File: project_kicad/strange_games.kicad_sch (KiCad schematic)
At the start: 131 parts, among them J1 Display, M1 Motor_DC, Q1 Si2302A, Q2 Q_Photo, Q3 Si2302A, Q4 Q_Photo, SW1 SW_Push, SW10 SW_Push, SW11 SW_Push, SW2 SW_Push, SW3 SW_Push, SW4 SW_Push, SW5 SW_Push, SW6 SW_Push, SW7 SW_Push, SW8 SW_Push, SW9 SW_Push, U1 charge controller, U2 boost converter, U3 LDL1117S33R, U4 ESP32-DEVKIT-V1, U5 TMP112xxDRL, U6 vibrating_sensor, U7 LSM6DS3, U8 MQ-135 gas sensor

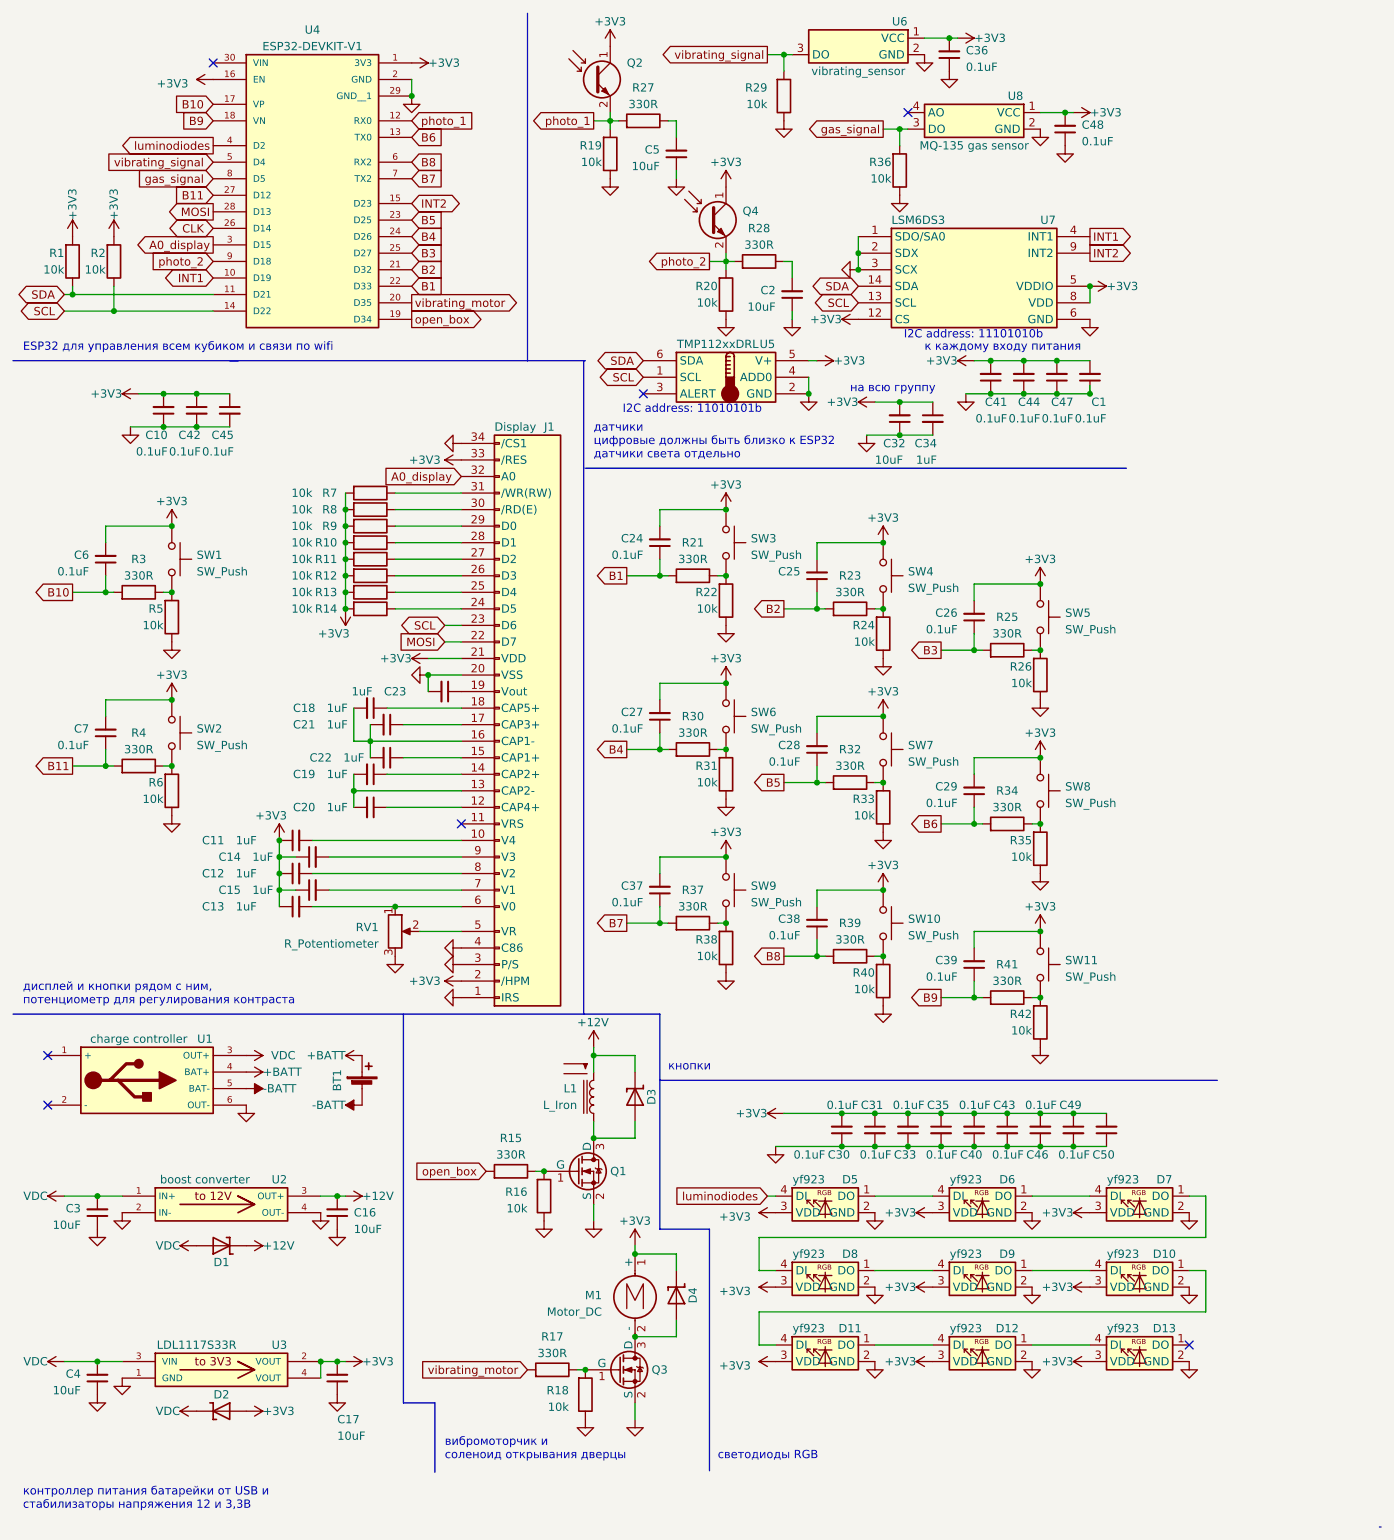
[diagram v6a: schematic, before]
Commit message: pcb changes
deleted resistor from unused pins because they take so much place
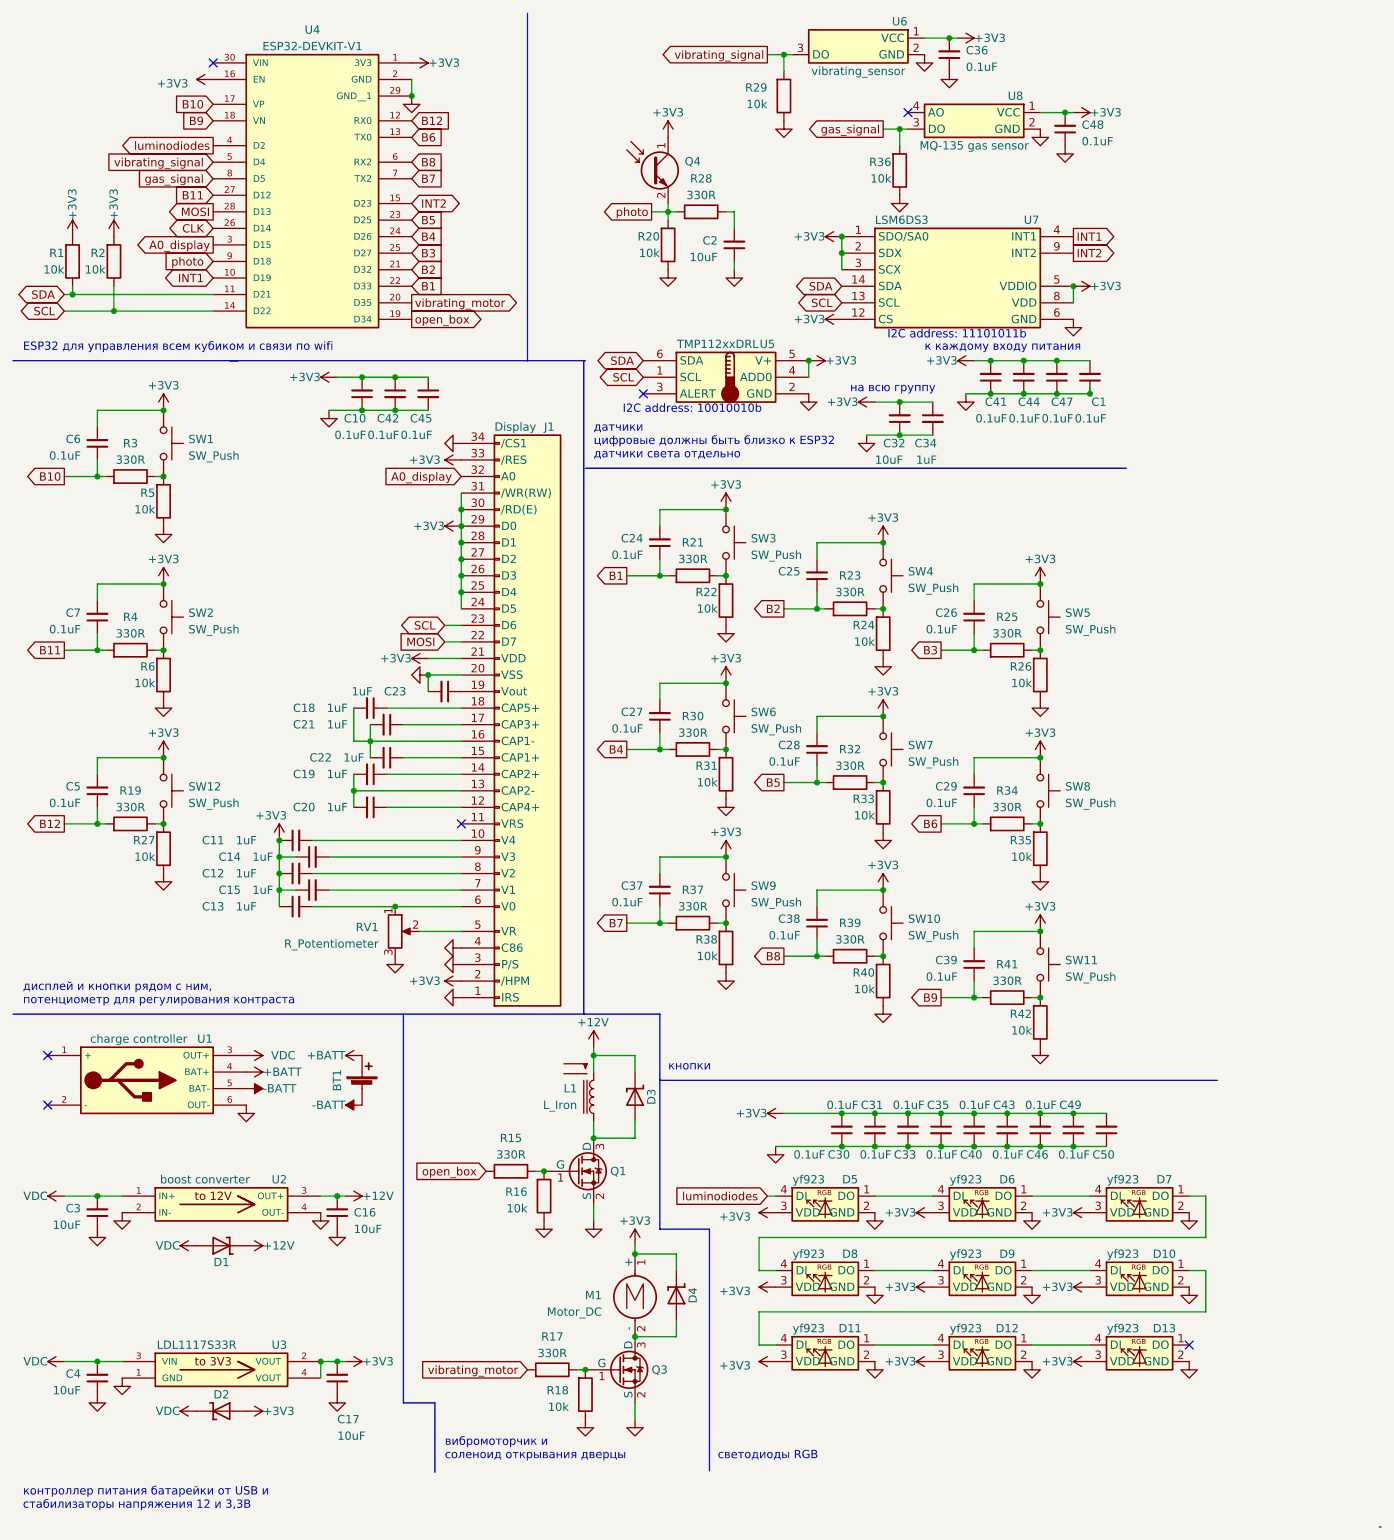
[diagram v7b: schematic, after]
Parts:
- removed Q2: Q_Photo, LED_THT:LED_D4.0mm, symbol Device:Q_Photo_NPN
- removed R10, R11, R12, R13, R14, R7, R8, R9: 10k_0805, PCM_4ms_Resistor:R_0805_2012Metric, symbol Library:1.2k_0603
- added SW12: SW_Push, Button_Switch_THT:SW_PUSH-12mm, symbol Switch:SW_Push
- C5: footprint PCM_Capacitor_SMD_AKL:C_0805_2012Metric -> PCM_Capacitor_SMD_AKL:C_0402_1005Metric; Capacity 10uF -> 0.1uF; Voltage 6.3V -> 10V
- R19: value 10k_0805 -> 330_0805; Display 10k -> 330R; Specifications 10K, 1%, 1/10W, 0805 -> 330, 1%, 1/10W, 0805
- R27: value 330_0805 -> 10k_0805; Display 330R -> 10k; Specifications 330, 1%, 1/10W, 0805 -> 10K, 1%, 1/10W, 0805
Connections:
- net +3V3: now also C5.2, J1.24 (D5), J1.25 (D4), J1.26 (D3), J1.27 (D2), J1.28 (D1), J1.29 (D0), J1.30 (/RD(E)), J1.31 (/WR(RW)), U5.4 (ADD0), U7.1 (SDO/SA0), U7.2 (SDX), U7.3 (SCX), SW12.1; no longer U7.10 (NC), U7.11 (NC)
- net GND: now also R27.1; no longer C5.1, R19.1, U5.4 (ADD0), U7.1 (SDO/SA0), U7.2 (SDX), U7.3 (SCX)
- net photo_1 renamed B12
- net B12: now also C5.1; no longer R27.2
- net photo_2 renamed photo
- new net: R19.1, R27.2, SW12.2
- new net: U7.10 (NC), U7.11 (NC)
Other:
- note added: "I2C address: 10010010b"
- note added: "I2C address: 11101011b"
- note removed: "I2C address: 11010101b"
- note removed: "I2C address: 11101010b"
- moved on the sheet: C10, C2, C42, C45, C6, C7, Q4, R20, R28, R3, R4, R5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

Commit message: pcb update
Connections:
- net B1: now also U4.3 (D15); no longer U4.22 (D33)
- net B10: now also U4.22 (D33); no longer U4.17 (VP)
- net B11: now also U4.23 (D25); no longer U4.27 (D12)
- net B12: now also U4.24 (D26); no longer U4.12 (RX0)
- net B2: now also U4.4 (D2); no longer U4.21 (D32)
- net B3: now also U4.5 (D4); no longer U4.25 (D27)
- net B4: now also U4.6 (RX2); no longer U4.24 (D26)
- net B5: now also U4.7 (TX2); no longer U4.23 (D25)
- net B6: now also U4.8 (D5); no longer U4.13 (TX0)
- net B7: now also U4.9 (D18); no longer U4.7 (TX2)
- net B8: now also U4.12 (RX0); no longer U4.6 (RX2)
- net B9: now also U4.13 (TX0); no longer U4.18 (VN)
- net CLK: now also J1.23 (D6)
- net SCL: no longer J1.23 (D6)
- net luminodiodes: now also U4.21 (D32); no longer D5.4 (DI), U4.4 (D2)
- net GasSensor: now reaches U8.4 (DO)
- net GasSensor: now also R36.2, U4.17 (VP)
- net A0_display renamed A0
- net A0: now also U4.27 (D12); no longer U4.3 (D15)
- removed net gas_signal: R36.2, U4.8 (D5), U8.3 (DO)
- net open_box renamed Door
- net Door: now also U4.20 (D35); no longer U4.19 (D34)
- net photo renamed PhotoSensor
- net PhotoSensor: now also U4.25 (D27); no longer U4.9 (D18)
- net vibrating_motor renamed VibrationMotor
- net VibrationMotor: now also U4.19 (D34); no longer U4.20 (D35)
- net vibrating_signal renamed VibrationsSensor
- net VibrationsSensor: no longer U4.5 (D4)
- new net Luminodiodes: D5.4 (DI)
- new net VibrationSensor: U4.18 (VN)
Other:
- moved on the sheet: D3, L1, Q1, R15, R16
